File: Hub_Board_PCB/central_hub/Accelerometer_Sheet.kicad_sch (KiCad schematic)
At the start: 3 parts, among them U3 MPU-6050

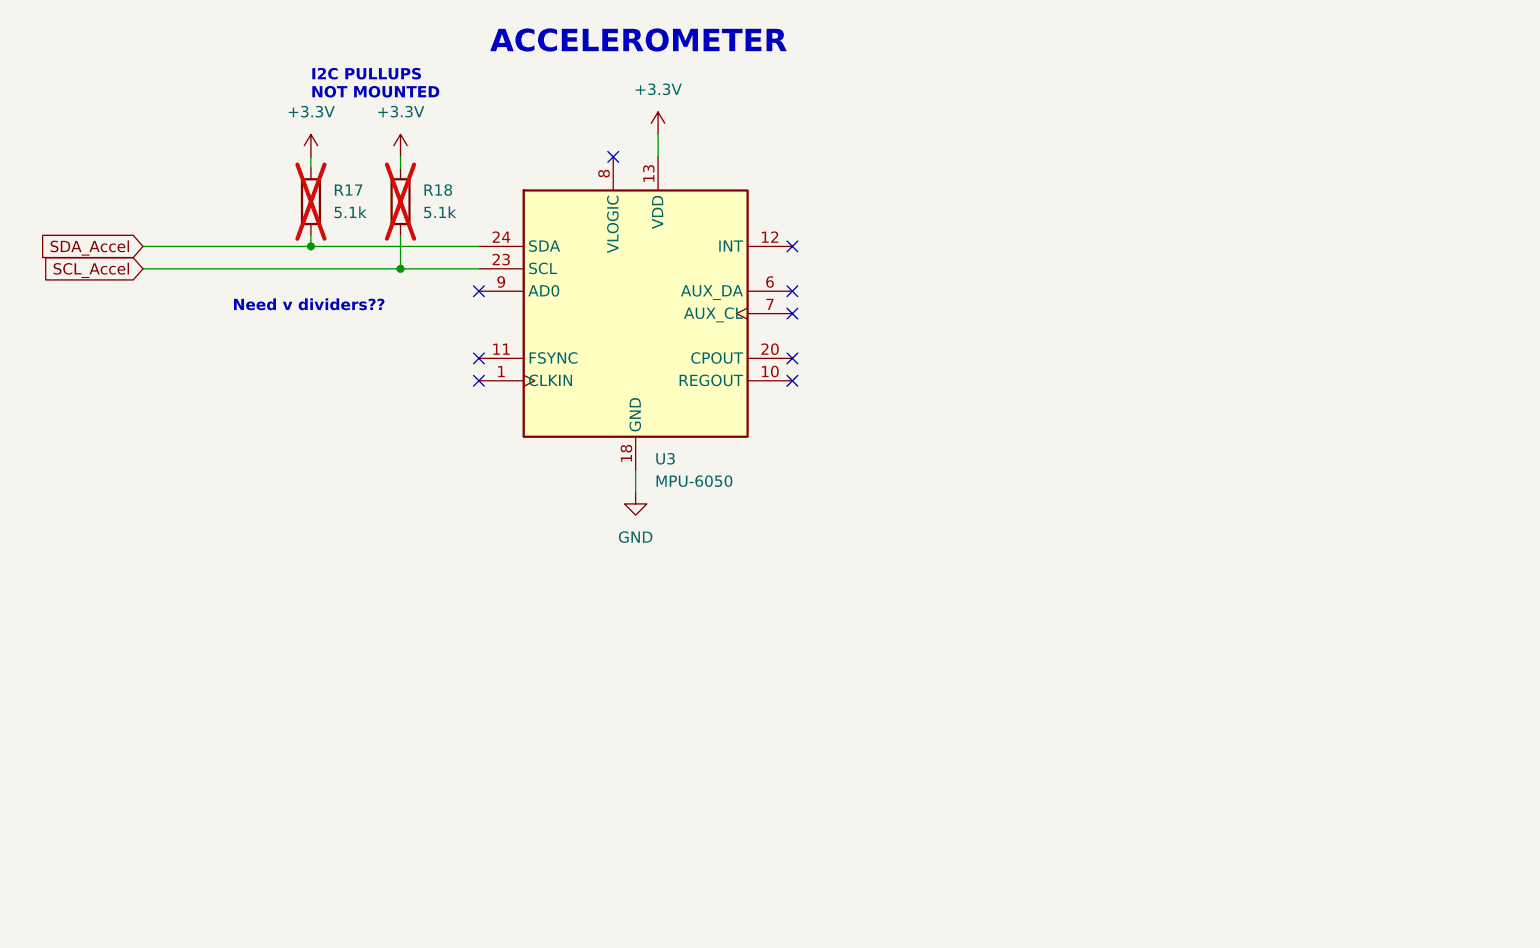
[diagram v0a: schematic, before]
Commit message: - added global net-labels and reorganized pages - 4.0" TFT SPI 480*320 V2.1 display may already have a level-shifter (actually has HR2046, touch screen controller) so may not need to include voltage dividers and NMOSes
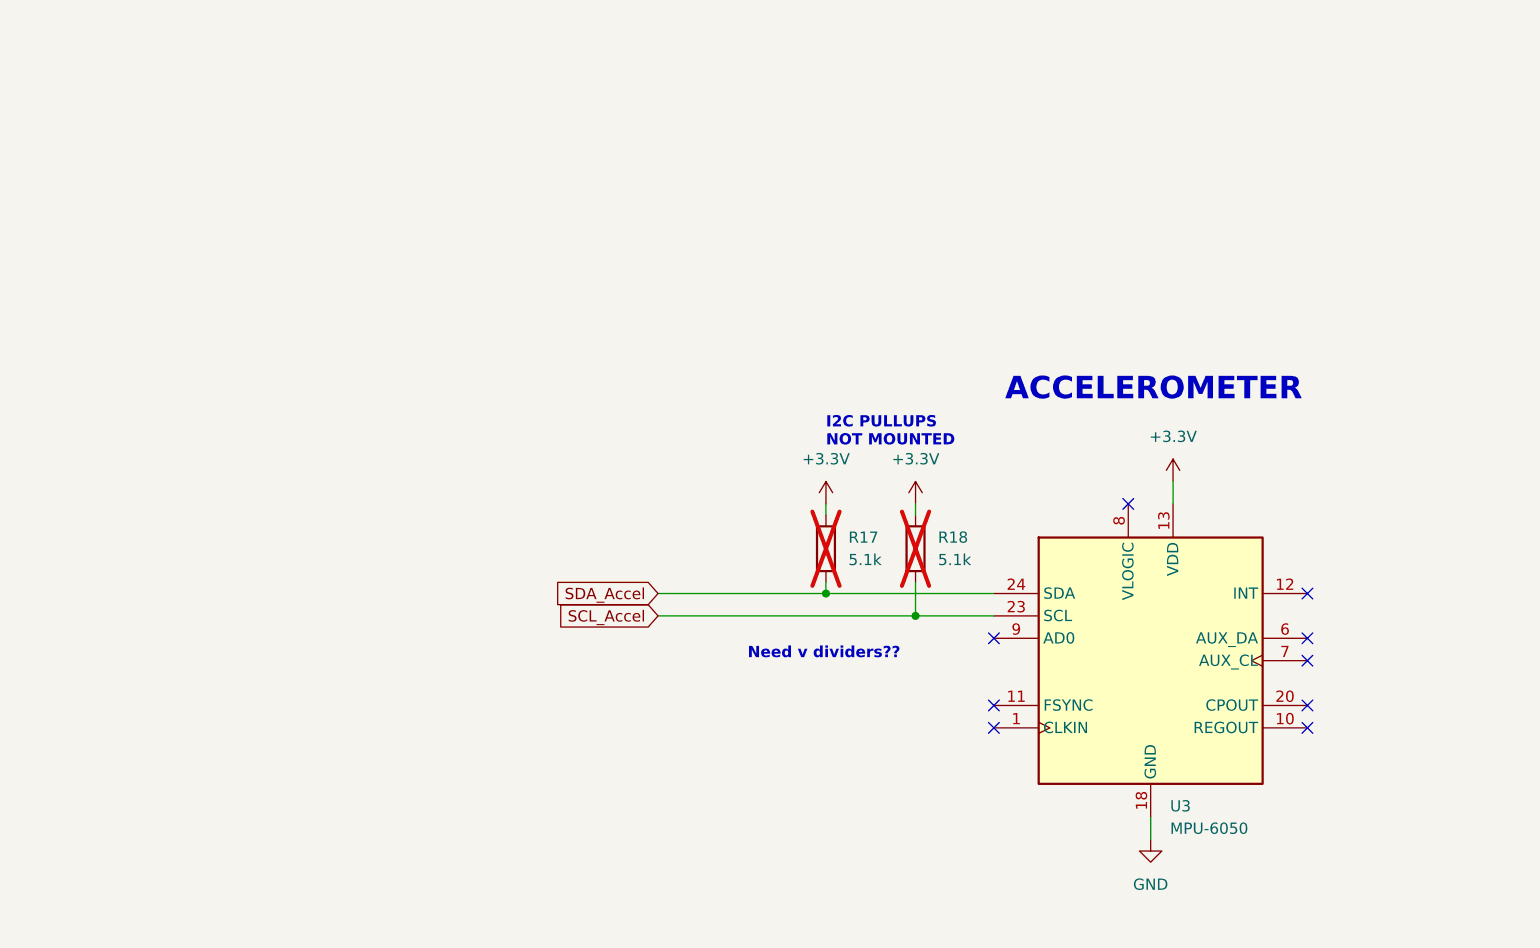
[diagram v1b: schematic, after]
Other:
- moved on the sheet: R17, R18, U3

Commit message: Added footprints for almost all components
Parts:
- R17, R18: footprint (none) -> Resistor_SMD:R_0603_1608Metric
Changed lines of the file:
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@@
       (effects (font (size 1.27 1.27)) (justify left))
     )
-    (property "Footprint" "" (at 125.222 87.63 90)
+    (property "Footprint" "Resistor_SMD:R_0603_1608Metric" (at 125.222 87.63 90)
       (effects (font (size 1.27 1.27)) hide)
     )
@@
         )
         (path "/0d9ec66e-0fbf-4d12-9b83-adf78971a00b/406a2e52-8680-458b-82c4-a5b80d2a411b"
-          (reference "R2") (unit 1)
+          (reference "R17") (unit 1)
         )
       )
@@
         )
         (path "/0d9ec66e-0fbf-4d12-9b83-adf78971a00b/406a2e52-8680-458b-82c4-a5b80d2a411b"
-          (reference "#PWR03") (unit 1)
+          (reference "#PWR033") (unit 1)
         )
       )
@@
       (effects (font (size 1.27 1.27)) (justify left))
     )
-    (property "Footprint" "" (at 115.062 87.63 90)
+    (property "Footprint" "Resistor_SMD:R_0603_1608Metric" (at 115.062 87.63 90)
       (effects (font (size 1.27 1.27)) hide)
     )
@@
         )
         (path "/0d9ec66e-0fbf-4d12-9b83-adf78971a00b/406a2e52-8680-458b-82c4-a5b80d2a411b"
-          (reference "R1") (unit 1)
+          (reference "R16") (unit 1)
         )
       )
@@
         )
         (path "/0d9ec66e-0fbf-4d12-9b83-adf78971a00b/406a2e52-8680-458b-82c4-a5b80d2a411b"
-          (reference "#PWR02") (unit 1)
+          (reference "#PWR032") (unit 1)
         )
       )
@@
         )
         (path "/0d9ec66e-0fbf-4d12-9b83-adf78971a00b/406a2e52-8680-458b-82c4-a5b80d2a411b"
-          (reference "#PWR04") (unit 1)
+          (reference "#PWR034") (unit 1)
         )
       )
@@
         )
         (path "/0d9ec66e-0fbf-4d12-9b83-adf78971a00b/406a2e52-8680-458b-82c4-a5b80d2a411b"
-          (reference "#PWR01") (unit 1)
+          (reference "#PWR031") (unit 1)
         )
       )
@@
         )
         (path "/0d9ec66e-0fbf-4d12-9b83-adf78971a00b/406a2e52-8680-458b-82c4-a5b80d2a411b"
-          (reference "U1") (unit 1)
-        )
-      )
+          (reference "U2") (unit 1)
+        )
+      )

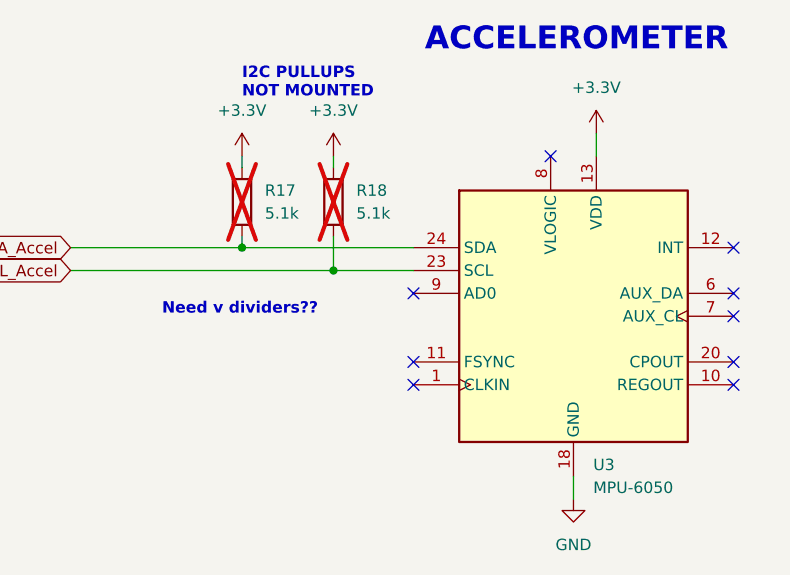
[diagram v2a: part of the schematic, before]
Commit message: Redid traces... might want auto trace lol
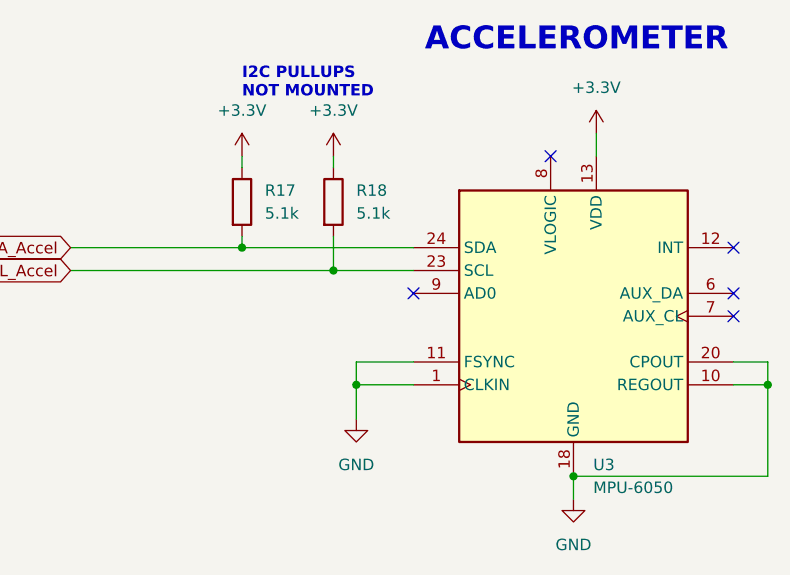
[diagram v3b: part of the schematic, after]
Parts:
- R17, R18: now fitted
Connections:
- net GND: now also U3.1 (CLKIN), U3.10 (REGOUT), U3.11 (FSYNC), U3.20 (CPOUT)
- no-connect marks 9 -> 5
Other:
- note removed: "Need v dividers??"
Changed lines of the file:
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@@
 (kicad_sch (version 20230121) (generator eeschema)
   (paper "A4")
+  (junction (at 153.67 118.11) (diameter 0) (color 0 0 0 0)
+  )
+  (junction (at 175.26 107.95) (diameter 0) (color 0 0 0 0)
+  )
+  (junction (at 129.54 107.95) (diameter 0) (color 0 0 0 0)
+  )
   (junction (at 116.84 92.71) (diameter 0) (color 0 0 0 0)
   )
   (junction (at 127 95.25) (diameter 0) (color 0 0 0 0)
   )
-  (no_connect (at 171.45 105.41))
-  (no_connect (at 171.45 107.95))
   (no_connect (at 171.45 100.33))
-  (no_connect (at 135.89 105.41))
   (no_connect (at 151.13 82.55))
   (no_connect (at 135.89 97.79))
-  (no_connect (at 135.89 107.95))
   (no_connect (at 171.45 97.79))
   (no_connect (at 171.45 92.71))
@@
     (stroke (width 0) (type default))
   )
+  (wire (pts (xy 175.26 105.41) (xy 175.26 107.95))
+    (stroke (width 0) (type default))
+  )
+  (wire (pts (xy 129.54 107.95) (xy 129.54 111.76))
+    (stroke (width 0) (type default))
+  )
   (wire (pts (xy 127 95.25) (xy 135.89 95.25))
     (stroke (width 0) (type default))
   )
+  (wire (pts (xy 129.54 105.41) (xy 135.89 105.41))
+    (stroke (width 0) (type default))
+  )
   (wire (pts (xy 116.84 82.55) (xy 116.84 83.82))
+    (stroke (width 0) (type default))
+  )
+  (wire (pts (xy 129.54 105.41) (xy 129.54 107.95))
     (stroke (width 0) (type default))
   )
@@
     (stroke (width 0) (type default))
   )
+  (wire (pts (xy 175.26 107.95) (xy 171.45 107.95))
+    (stroke (width 0) (type default))
+  )
+  (wire (pts (xy 153.67 118.11) (xy 175.26 118.11))
+    (stroke (width 0) (type default))
+  )
+  (wire (pts (xy 171.45 105.41) (xy 175.26 105.41))
+    (stroke (width 0) (type default))
+  )
   (wire (pts (xy 127 91.44) (xy 127 95.25))
+    (stroke (width 0) (type default))
+  )
+  (wire (pts (xy 135.89 107.95) (xy 129.54 107.95))
     (stroke (width 0) (type default))
   )
@@
     (stroke (width 0) (type default))
   )
+  (wire (pts (xy 175.26 118.11) (xy 175.26 107.95))
+    (stroke (width 0) (type default))
+  )
   (wire (pts (xy 97.79 95.25) (xy 127 95.25))
     (stroke (width 0) (type default))
-  )
-  (text "Need v dividers??\n" (at 107.95 100.33 0)
-    (effects (font (size 1.27 1.27) (thickness 0.254) bold) (justify left bottom))
   )
   (text "ACCELEROMETER\n" (at 137.16 71.12 0)
@@
     )
   )
+  (symbol (lib_id "power:GND") (at 129.54 111.76 0) (unit 1)
+    (in_bom yes) (on_board yes) (dnp no) (fields_autoplaced)
+    (property "Reference" "#PWR042" (at 129.54 118.11 0)
+      (effects (font (size 1.27 1.27)) hide)
+    )
+    (property "Value" "GND" (at 129.54 116.84 0)
+      (effects (font (size 1.27 1.27)))
+    )
+    (property "Footprint" "" (at 129.54 111.76 0)
+      (effects (font (size 1.27 1.27)) hide)
+    )
+    (property "Datasheet" "" (at 129.54 111.76 0)
+      (effects (font (size 1.27 1.27)) hide)
+    )
+    (pin "1")
+    (instances
+      (project "central_hub"
+        (path "/0d9ec66e-0fbf-4d12-9b83-adf78971a00b"
+          (reference "#PWR042") (unit 1)
+        )
+        (path "/0d9ec66e-0fbf-4d12-9b83-adf78971a00b/4fb60496-ee10-4e45-a75e-a49c2c8afc68"
+          (reference "#PWR0119") (unit 1)
+        )
+        (path "/0d9ec66e-0fbf-4d12-9b83-adf78971a00b/406a2e52-8680-458b-82c4-a5b80d2a411b"
+          (reference "#PWR072") (unit 1)
+        )
+      )
+    )
+  )
   (symbol (lib_id "Device:R") (at 127 87.63 0) (unit 1)
-    (in_bom yes) (on_board yes) (dnp yes) (fields_autoplaced)
+    (in_bom yes) (on_board yes) (dnp no) (fields_autoplaced)
     (property "Reference" "R18" (at 129.54 86.36 0)
       (effects (font (size 1.27 1.27)) (justify left))
@@
   )
   (symbol (lib_id "Device:R") (at 116.84 87.63 0) (unit 1)
-    (in_bom yes) (on_board yes) (dnp yes) (fields_autoplaced)
+    (in_bom yes) (on_board yes) (dnp no) (fields_autoplaced)
     (property "Reference" "R17" (at 119.38 86.36 0)
       (effects (font (size 1.27 1.27)) (justify left))

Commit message: Added new connectors as per brandons new shifters
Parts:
- R17, R18: value 5.1k -> 4.7k
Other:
- note added: "I2C PULLUPS"
- note removed: "I2C PULLUPS NOT MOUNTED"
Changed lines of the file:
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@@
     (effects (font (size 2.54 2.54) (thickness 0.254) bold) (justify left bottom))
   )
-  (text "I2C PULLUPS\nNOT MOUNTED" (at 116.84 76.2 0)
+  (text "I2C PULLUPS" (at 116.84 76.2 0)
     (effects (font (size 1.27 1.27) (thickness 0.254) bold) (justify left bottom))
   )
@@
       (effects (font (size 1.27 1.27)) (justify left))
     )
-    (property "Value" "5.1k" (at 129.54 88.9 0)
+    (property "Value" "4.7k" (at 129.54 88.9 0)
       (effects (font (size 1.27 1.27)) (justify left))
     )
@@
       (effects (font (size 1.27 1.27)) (justify left))
     )
-    (property "Value" "5.1k" (at 119.38 88.9 0)
+    (property "Value" "4.7k" (at 119.38 88.9 0)
       (effects (font (size 1.27 1.27)) (justify left))
     )

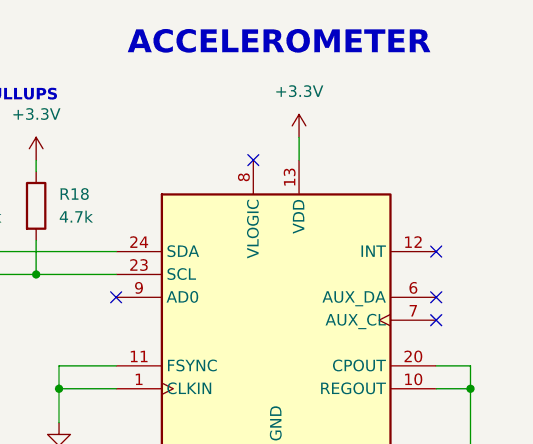
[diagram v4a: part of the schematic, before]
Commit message: Added cap on accel chip and switched power connector
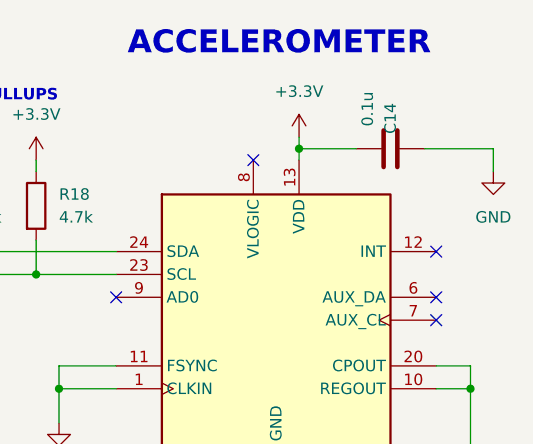
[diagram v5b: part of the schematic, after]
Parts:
- added C14: 0.1u, Capacitor_SMD:C_0603_1608Metric, symbol Device:C
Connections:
- net +3.3V: now also C14.2
- net GND: now also C14.1
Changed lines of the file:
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@@
   (junction (at 153.67 118.11) (diameter 0) (color 0 0 0 0)
+  )
+  (junction (at 156.21 81.28) (diameter 0) (color 0 0 0 0)
   )
   (junction (at 175.26 107.95) (diameter 0) (color 0 0 0 0)
@@
   (no_connect (at 171.45 97.79))
   (no_connect (at 171.45 92.71))
-  (wire (pts (xy 156.21 80.01) (xy 156.21 82.55))
+  (wire (pts (xy 156.21 80.01) (xy 156.21 81.28))
     (stroke (width 0) (type default))
   )
@@
     (stroke (width 0) (type default))
   )
+  (wire (pts (xy 170.18 81.28) (xy 177.8 81.28))
+    (stroke (width 0) (type default))
+  )
   (wire (pts (xy 129.54 105.41) (xy 135.89 105.41))
     (stroke (width 0) (type default))
@@
     (stroke (width 0) (type default))
   )
+  (wire (pts (xy 162.56 81.28) (xy 156.21 81.28))
+    (stroke (width 0) (type default))
+  )
   (wire (pts (xy 153.67 118.11) (xy 153.67 120.65))
     (stroke (width 0) (type default))
   )
+  (wire (pts (xy 156.21 81.28) (xy 156.21 82.55))
+    (stroke (width 0) (type default))
+  )
   (wire (pts (xy 175.26 107.95) (xy 171.45 107.95))
     (stroke (width 0) (type default))
@@
   )
   (wire (pts (xy 135.89 107.95) (xy 129.54 107.95))
+    (stroke (width 0) (type default))
+  )
+  (wire (pts (xy 177.8 81.28) (xy 177.8 83.82))
     (stroke (width 0) (type default))
   )
@@
     )
   )
+  (symbol (lib_id "power:GND") (at 177.8 83.82 0) (unit 1)
+    (in_bom yes) (on_board yes) (dnp no) (fields_autoplaced)
+    (property "Reference" "#PWR042" (at 177.8 90.17 0)
+      (effects (font (size 1.27 1.27)) hide)
+    )
+    (property "Value" "GND" (at 177.8 88.9 0)
+      (effects (font (size 1.27 1.27)))
+    )
+    (property "Footprint" "" (at 177.8 83.82 0)
+      (effects (font (size 1.27 1.27)) hide)
+    )
+    (property "Datasheet" "" (at 177.8 83.82 0)
+      (effects (font (size 1.27 1.27)) hide)
+    )
+    (pin "1")
+    (instances
+      (project "central_hub"
+        (path "/0d9ec66e-0fbf-4d12-9b83-adf78971a00b"
+          (reference "#PWR042") (unit 1)
+        )
+        (path "/0d9ec66e-0fbf-4d12-9b83-adf78971a00b/4fb60496-ee10-4e45-a75e-a49c2c8afc68"
+          (reference "#PWR0119") (unit 1)
+        )
+        (path "/0d9ec66e-0fbf-4d12-9b83-adf78971a00b/406a2e52-8680-458b-82c4-a5b80d2a411b"
+          (reference "#PWR045") (unit 1)
+        )
+      )
+    )
+  )
   (symbol (lib_id "Device:R") (at 127 87.63 0) (unit 1)
     (in_bom yes) (on_board yes) (dnp no) (fields_autoplaced)
@@
         )
       )
+    )
+  )
+  (symbol (lib_id "Device:C") (at 166.37 81.28 270) (unit 1)
+    (in_bom yes) (on_board yes) (dnp no)
+    (property "Reference" "C14" (at 166.37 76.2 0)
+      (effects (font (size 1.27 1.27)) (justify left))
+    )
+    (property "Value" "0.1u" (at 163.83 74.93 0)
+      (effects (font (size 1.27 1.27)) (justify left))
+    )
+    (property "Footprint" "Capacitor_SMD:C_0603_1608Metric" (at 162.56 82.2452 0)
+      (effects (font (size 1.27 1.27)) hide)
+    )
+    (property "Datasheet" "~" (at 166.37 81.28 0)
+      (effects (font (size 1.27 1.27)) hide)
+    )
+    (pin "1")
+    (pin "2")
+    (instances
+      (project "central_hub"
+        (path "/0d9ec66e-0fbf-4d12-9b83-adf78971a00b/a9a7affa-d8a7-4dcd-8fe3-0de6a2b29bd6"
+          (reference "C14") (unit 1)
+        )
+        (path "/0d9ec66e-0fbf-4d12-9b83-adf78971a00b/406a2e52-8680-458b-82c4-a5b80d2a411b"
+          (reference "C15") (unit 1)
+        )
+      )
+      (project "motor_board_pcb"
+        (path "/4ad82a24-c992-45c9-b523-12e12bcd6ced"
+          (reference "C?") (unit 1)
+        )
+        (path "/4ad82a24-c992-45c9-b523-12e12bcd6ced/63c66207-e5d4-4f6f-af8f-451675dc3930"
+          (reference "C14") (unit 1)
+        )
+      )
